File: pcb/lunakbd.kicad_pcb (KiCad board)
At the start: 2 copper layers, 134.4 x 112.7 mm, 64 parts, among them J1 TRRS-PJ-320A, J2 Battery_Socket, J3 Conn_Display, SW1 Switch, SW10 Switch, SW11 Switch, SW12 Switch, SW13 Switch, SW14 Switch, SW15 Switch, SW16 Switch, SW17 Switch, SW18 Switch, SW19 Switch, SW2 Switch, SW20 Switch, SW21 Switch, SW22 Switch, SW23 Switch, SW24 Switch, SW25 Switch, SW26 Switch, SW27 Switch, SW28 Switch, SW29 RotaryEncoder_SW, SW3 Switch, SW30 Reset_Button, SW31 Battery_Switch, SW4 Switch, SW5 Switch, SW6 Switch, SW7 Switch, SW8 Switch, SW9 Switch, U1 SuperMini_nRF52840_H_USBdn

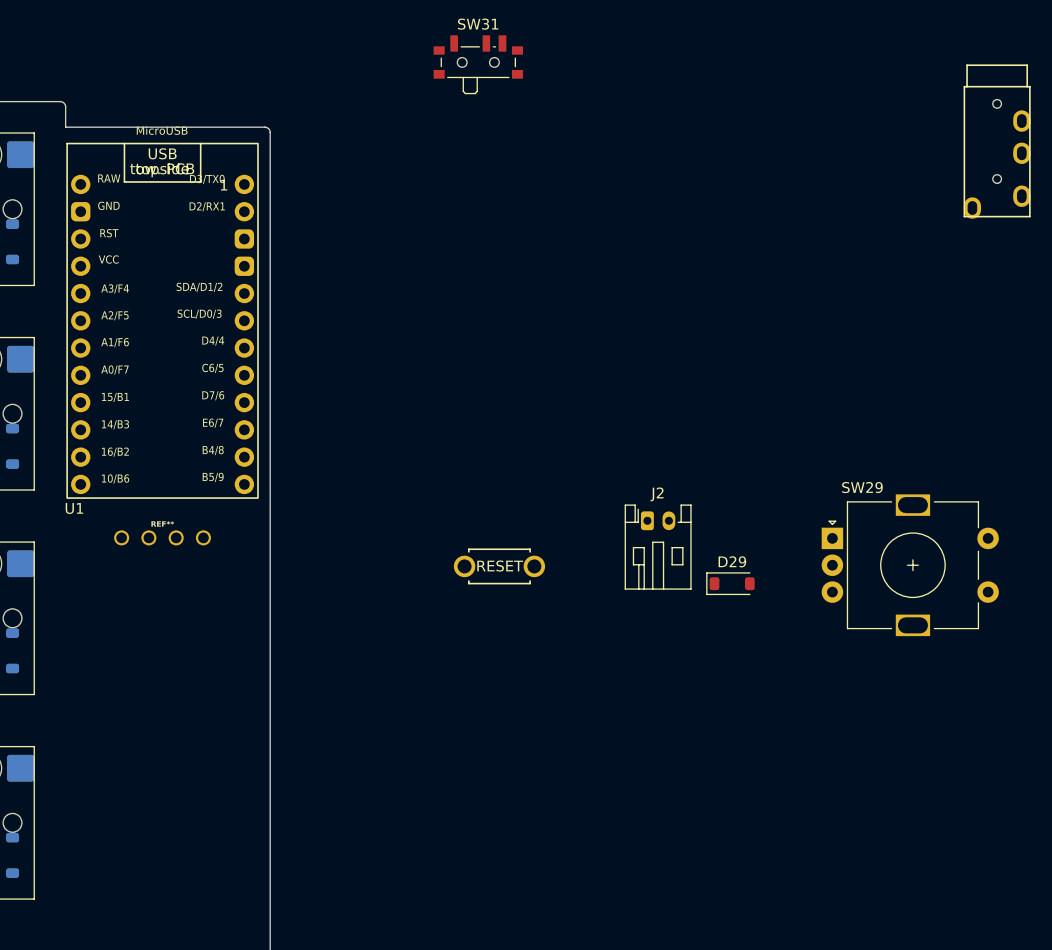
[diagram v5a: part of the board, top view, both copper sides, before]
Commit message: feat: place rotatory encoder and centralize oled display
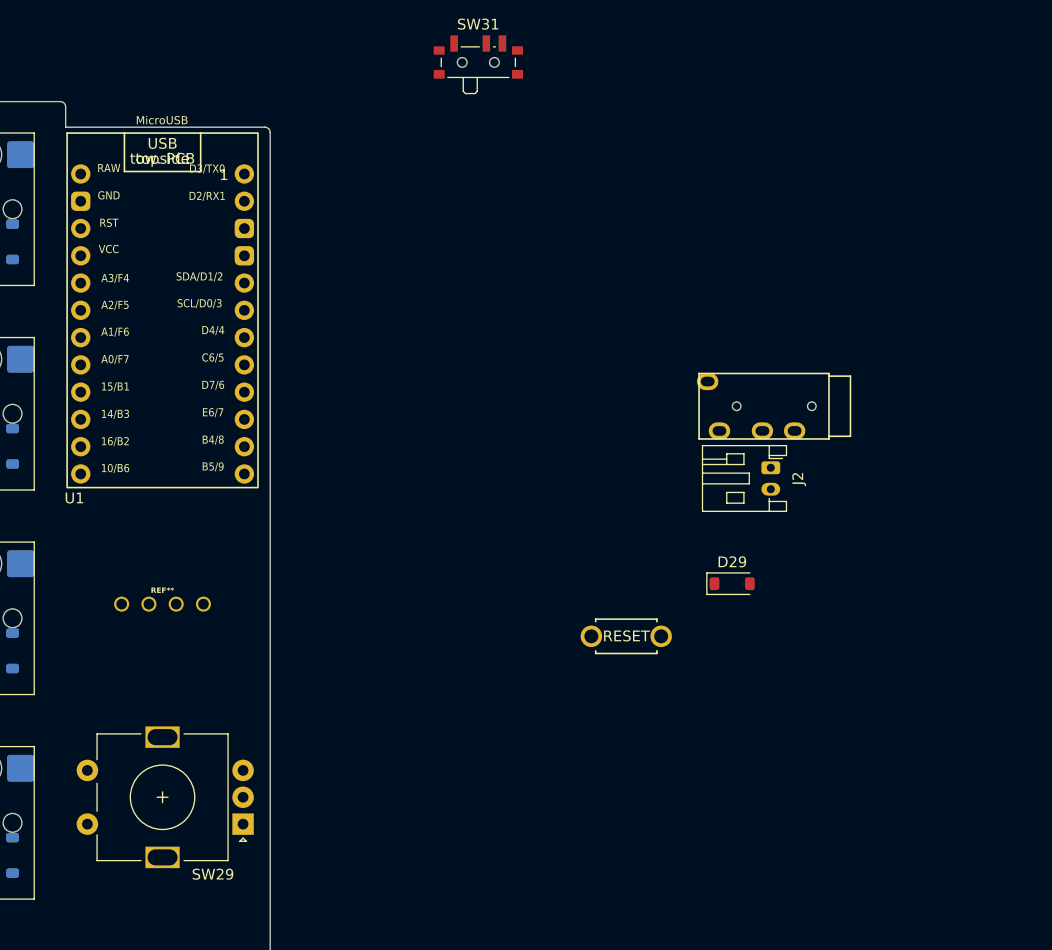
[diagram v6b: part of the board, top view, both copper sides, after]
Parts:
- moved SW29 61.0 mm to (198.0, 107.3), turned to 180 degrees
- moved J1 33.6 mm to (252.6, 68.4), turned to -90 degrees
- moved SW30 13.5 mm to (233.7, 89.8)
- moved J2 12.5 mm to (247.2, 74.1), turned to -90 degrees
- moved J3 6.17 mm to (190.5, 86.8)
- moved U1 0.97 mm to (190.5, 60.7)
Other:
- outline, holes or cut-outs redrawn

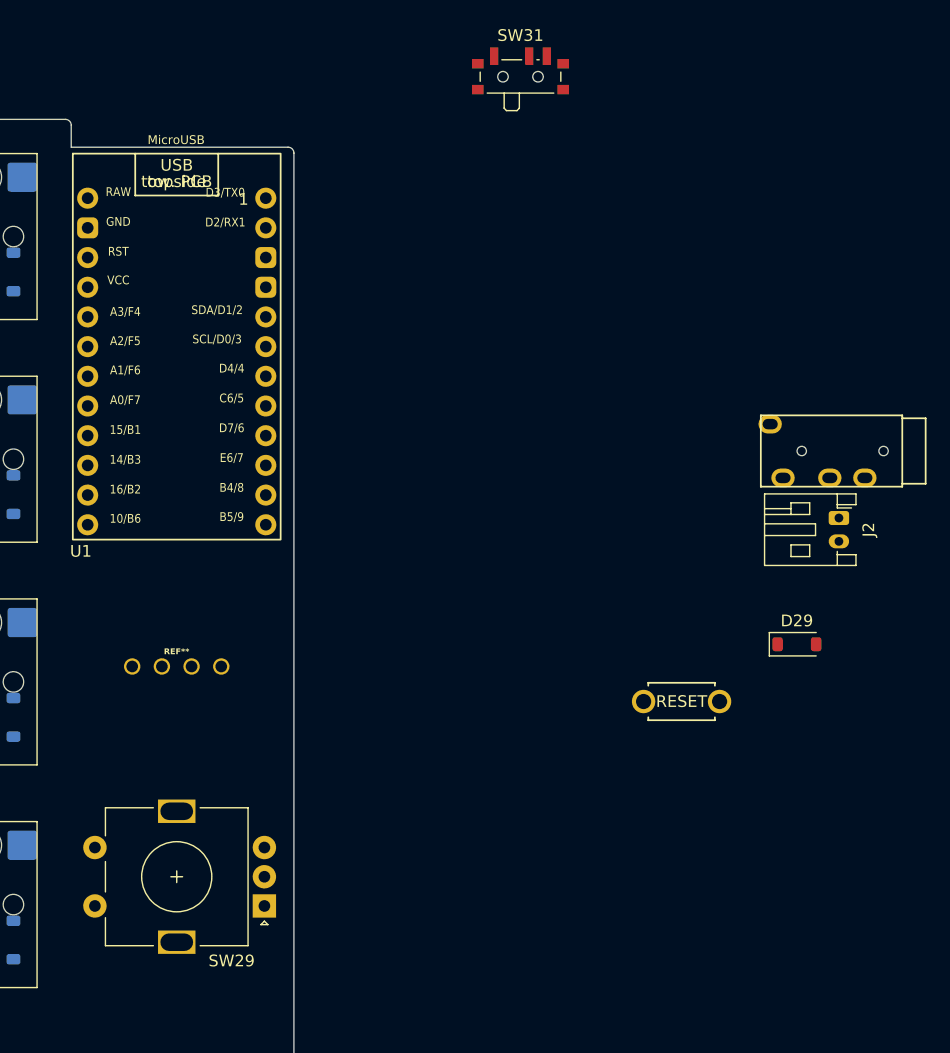
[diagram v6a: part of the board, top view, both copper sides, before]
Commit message: feat: place trrs, battery socket and reset button
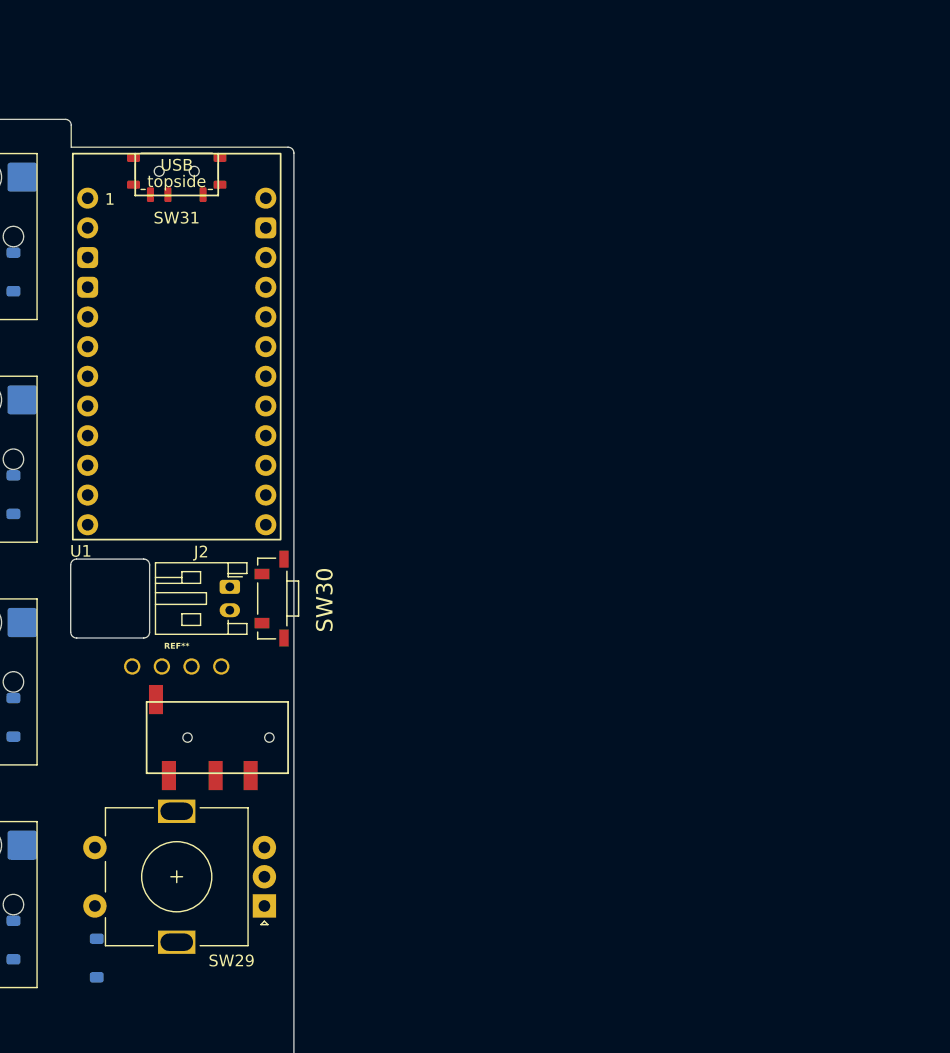
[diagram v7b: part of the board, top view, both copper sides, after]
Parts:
- D29: moved to B.Cu
- J1: value TRRS-PJ-320A -> TRRS-PJ-320D; footprint Keebio-Parts:TRRS-PJ-320A-no-Fmask -> Keebio-Parts:TRRS-PJ-320D
- SW30: footprint kbd:ResetSW -> kbd:SW_TL3330AF130QG
- SW31: footprint Button_Switch_SMD:SW_SPDT_PCM12 -> PCM_marbastlib-various:SW_MSK12C02-HB
- U1: value SuperMini_nRF52840_H_USBdn -> ProMicro; footprint PCM_marbastlib-xp-promicroish:SuperMini_nRF52840_H_USBdn -> PCM_marbastlib-xp-promicroish:SuperMini_nRF52840_H_USBup
- moved D29 65.6 mm to (183.7, 111.7), turned to 90 degrees
- moved J1 58.0 mm to (200.0, 92.9)
- moved J2 52.4 mm to (195.0, 80.0)
- moved SW30 36.1 mm to (198.7, 81.0), turned to 90 degrees
- moved SW31 30.6 mm to (190.5, 44.4)
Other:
- outline, holes or cut-outs redrawn

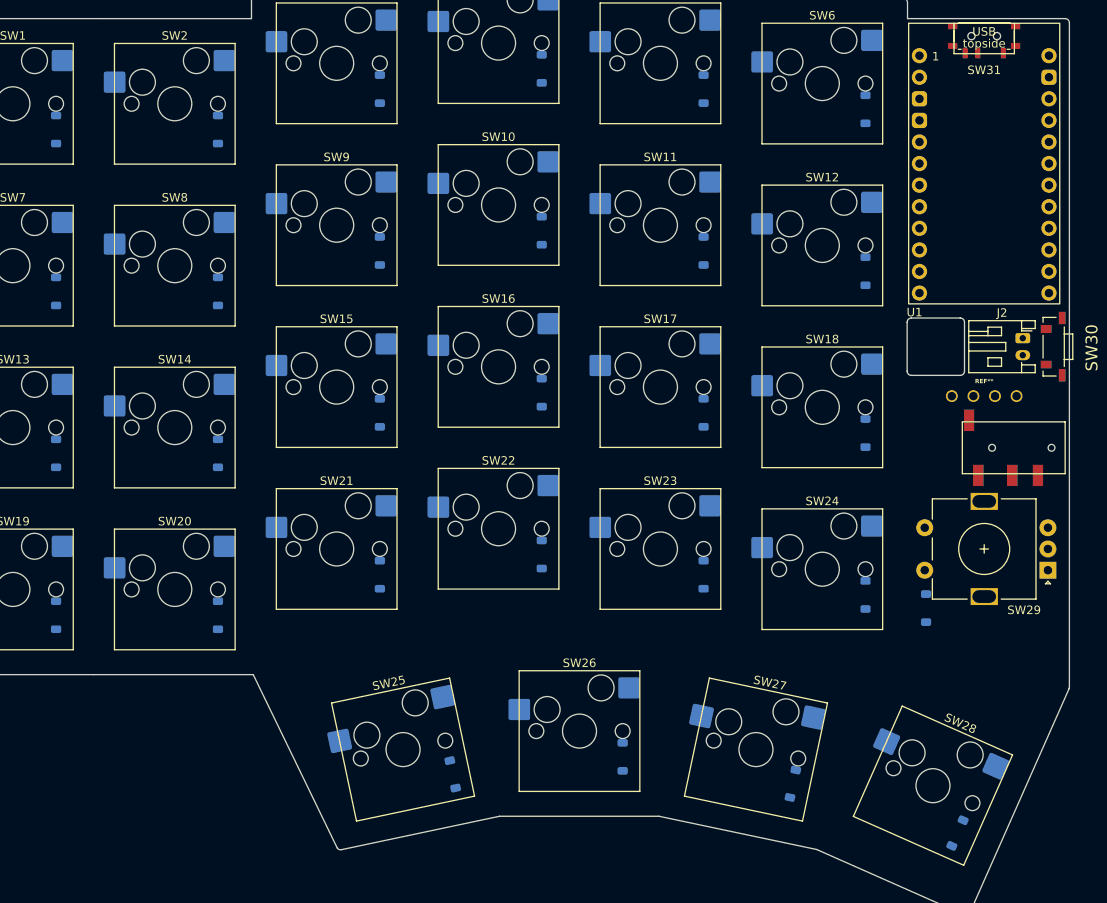
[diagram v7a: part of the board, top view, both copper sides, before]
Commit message: feat: update diode positions
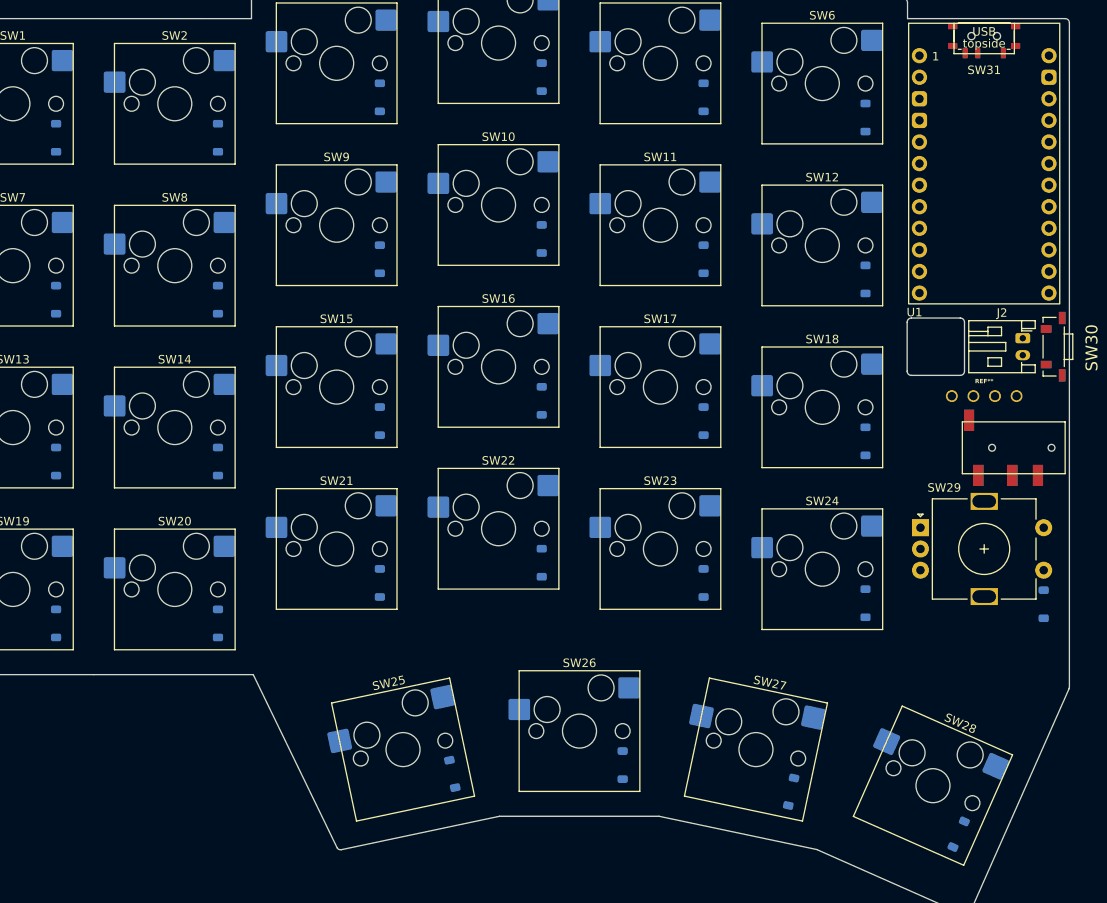
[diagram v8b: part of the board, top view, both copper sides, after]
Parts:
- moved SW29 15.8 mm to (183.0, 102.3), turned to 0 degrees
- moved D29 13.8 mm to (197.5, 111.3)
- moved D1 0.97 mm to (81.3, 56.4)
- moved D2 0.97 mm to (100.3, 56.4)
- moved D10 0.97 mm to (138.4, 68.3)
- moved D11 0.97 mm to (157.5, 70.7)
- moved D12 0.97 mm to (176.5, 73.1)
- moved D13 0.97 mm to (81.3, 94.5)
- moved D14 0.97 mm to (100.3, 94.5)
- moved D15 0.97 mm to (119.4, 89.7)
- moved D16 0.97 mm to (138.4, 87.3)
- moved D17 0.97 mm to (157.5, 89.7)
- moved D18 0.97 mm to (176.5, 92.1)
- moved D19 0.97 mm to (81.3, 113.5)
- moved D20 0.97 mm to (100.3, 113.5)
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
